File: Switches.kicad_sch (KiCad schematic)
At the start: 36 parts, among them SW10 SW_SPST, SW11 SW_SPST, SW12 SW_SPST, SW13 SW_SPST, SW14 SW_SPST, SW15 SW_SPST, SW16 SW_SPST, SW17 SW_SPST, SW18 Rotary, SW19 Rotary, SW2 SW_SPST, SW3 SW_SPST, SW4 SW_SPST, SW5 SW_SPST, SW6 SW_SPST, SW7 SW_SPST, SW8 SW_SPST, SW9 SW_SPST

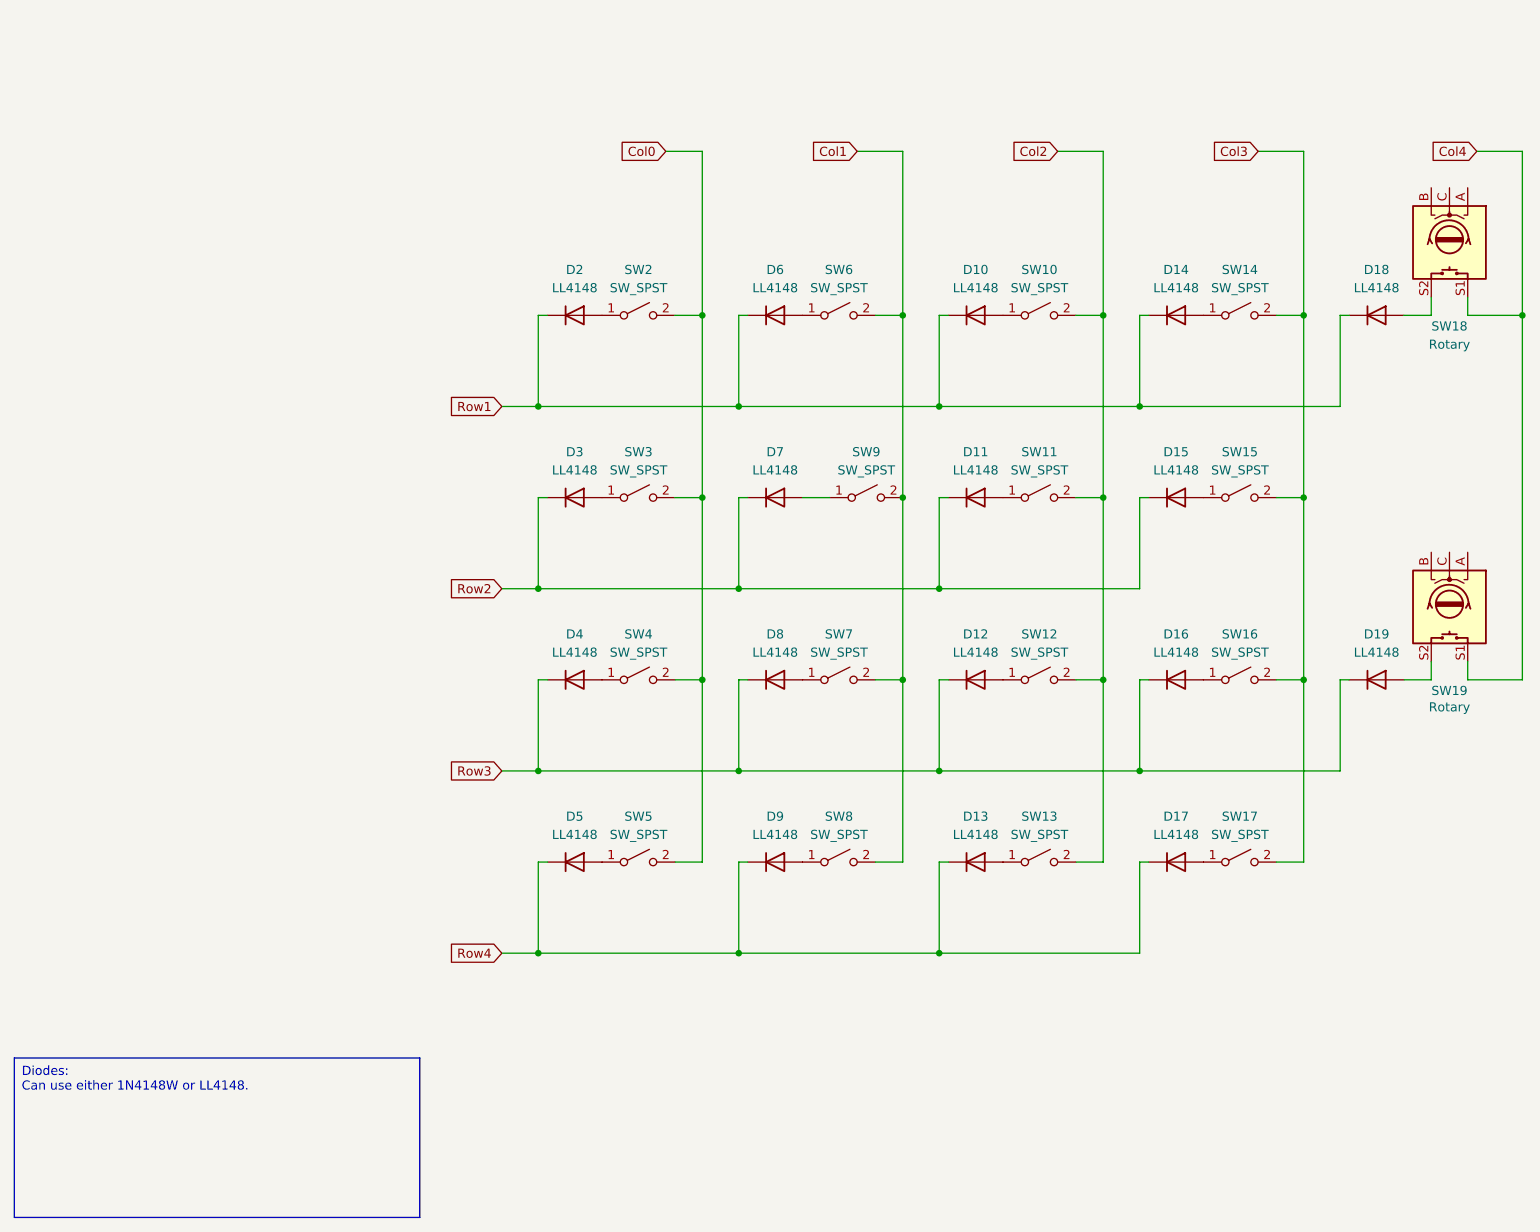
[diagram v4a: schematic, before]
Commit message: Select last few components, add and cleanup footprints
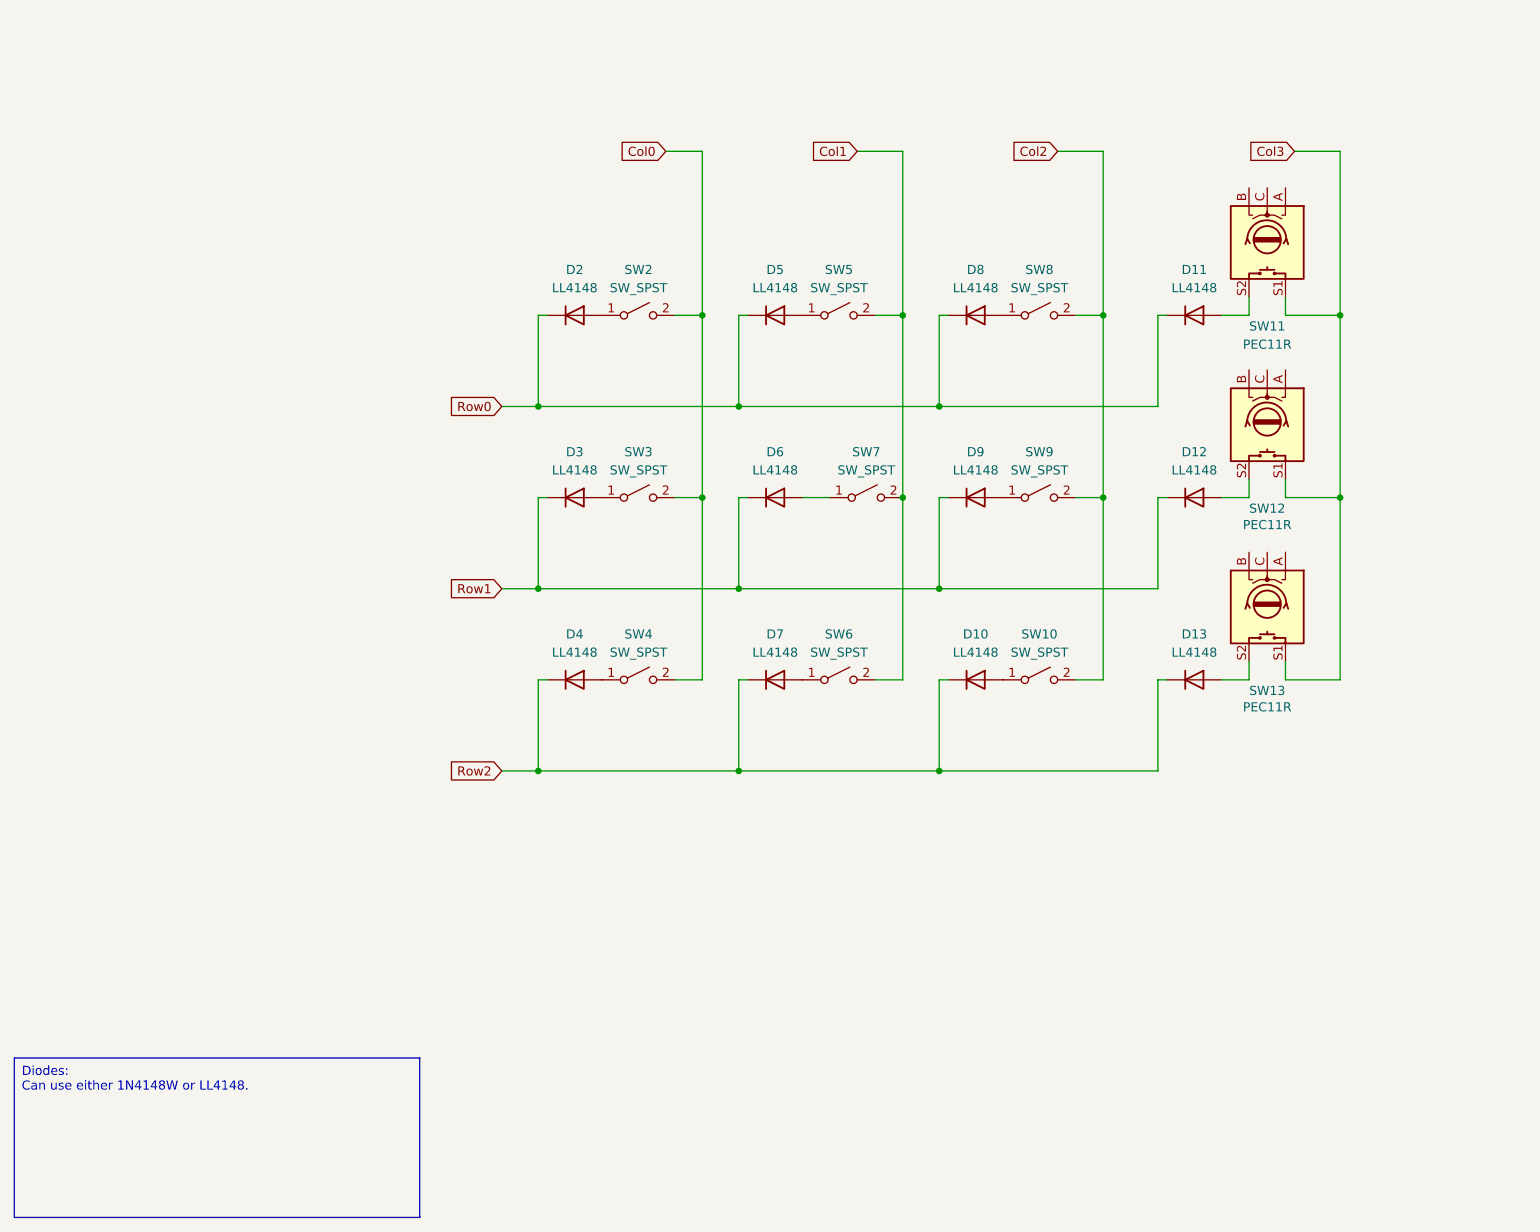
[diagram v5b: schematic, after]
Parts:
- removed D13, D14, D15, D16, D17, D5, D9: LL4148, Diode_SMD:D_MiniMELF, symbol Diode:LL4148
- removed SW13, SW14, SW15, SW16, SW17, SW5, SW8: SW_SPST, PCM_Switch_Keyboard_Cherry_MX:SW_Cherry_MX_PCB_1.00u, symbol Switch:SW_SPST
- added D12: LL4148, Diode_SMD:D_MiniMELF, symbol Diode:LL4148
- added SW12: PEC11R, Mad_Footprints:RotaryEncoder_Bourns_Vertical_PEC12R-3x17F-Sxxxx, symbol Device:RotaryEncoder_Switch
- SW10: renamed from SW12; footprint PCM_Switch_Keyboard_Cherry_MX:SW_Cherry_MX_PCB_1.00u -> Mad_Footprints:SW_Hotswap_Kailh_MX_1.00u
- SW11: renamed from SW18; value Rotary -> PEC11R; footprint (none) -> Mad_Footprints:RotaryEncoder_Bourns_Vertical_PEC12R-3x17F-Sxxxx; MPN (none) -> PEC11R-4215F-S0024; Manufacturer (none) -> Bourns Inc.; Price (none) -> $3.37; Rating (none) -> ROTARY ENCODER MECHANICAL 24PPR; Supplier (none) -> Digikey; Supplier PN (none) -> PEC11R-4215F-S0024-ND
- SW13: renamed from SW19; value Rotary -> PEC11R; footprint (none) -> Mad_Footprints:RotaryEncoder_Bourns_Vertical_PEC12R-3x17F-Sxxxx; MPN (none) -> PEC11R-4215F-S0024; Manufacturer (none) -> Bourns Inc.; Price (none) -> $3.37; Rating (none) -> ROTARY ENCODER MECHANICAL 24PPR; Supplier (none) -> Digikey; Supplier PN (none) -> PEC11R-4215F-S0024-ND
- SW2, SW3, SW4: footprint PCM_Switch_Keyboard_Cherry_MX:SW_Cherry_MX_PCB_1.00u -> Mad_Footprints:SW_Hotswap_Kailh_MX_1.00u
- SW5: renamed from SW6; footprint PCM_Switch_Keyboard_Cherry_MX:SW_Cherry_MX_PCB_1.00u -> Mad_Footprints:SW_Hotswap_Kailh_MX_1.00u
- SW6: renamed from SW7; footprint PCM_Switch_Keyboard_Cherry_MX:SW_Cherry_MX_PCB_1.00u -> Mad_Footprints:SW_Hotswap_Kailh_MX_1.00u
- SW7: renamed from SW9; footprint PCM_Switch_Keyboard_Cherry_MX:SW_Cherry_MX_PCB_1.00u -> Mad_Footprints:SW_Hotswap_Kailh_MX_1.00u
- SW8: renamed from SW10; footprint PCM_Switch_Keyboard_Cherry_MX:SW_Cherry_MX_PCB_1.00u -> Mad_Footprints:SW_Hotswap_Kailh_MX_1.00u
- SW9: renamed from SW11; footprint PCM_Switch_Keyboard_Cherry_MX:SW_Cherry_MX_PCB_1.00u -> Mad_Footprints:SW_Hotswap_Kailh_MX_1.00u
- renumbered D12 to D10, D18 to D11, D19 to D13, D6 to D5, D7 to D6, D8 to D7, D10 to D8, D11 to D9
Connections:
- net Col4 is gone; now on net Col3: SW11.S1, SW13.S1
- net Row3 is gone; now on net Row2: D10.1 (K), D13.1 (K), D4.1 (K), D7.1 (K)
- net Col3: now also SW12.S1
- net Row1: now also D3.1 (K), D6.1 (K), D9.1 (K), D12.1 (K); no longer D11.1 (K), D2.1 (K), D5.1 (K), D8.1 (K)
- net Row2: no longer D3.1 (K), D6.1 (K), D9.1 (K)
- new net: D12.2 (A), SW12.S2
- new net Row0: D11.1 (K), D2.1 (K), D5.1 (K), D8.1 (K)
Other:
- moved on the sheet: D11, D13, SW11, SW13

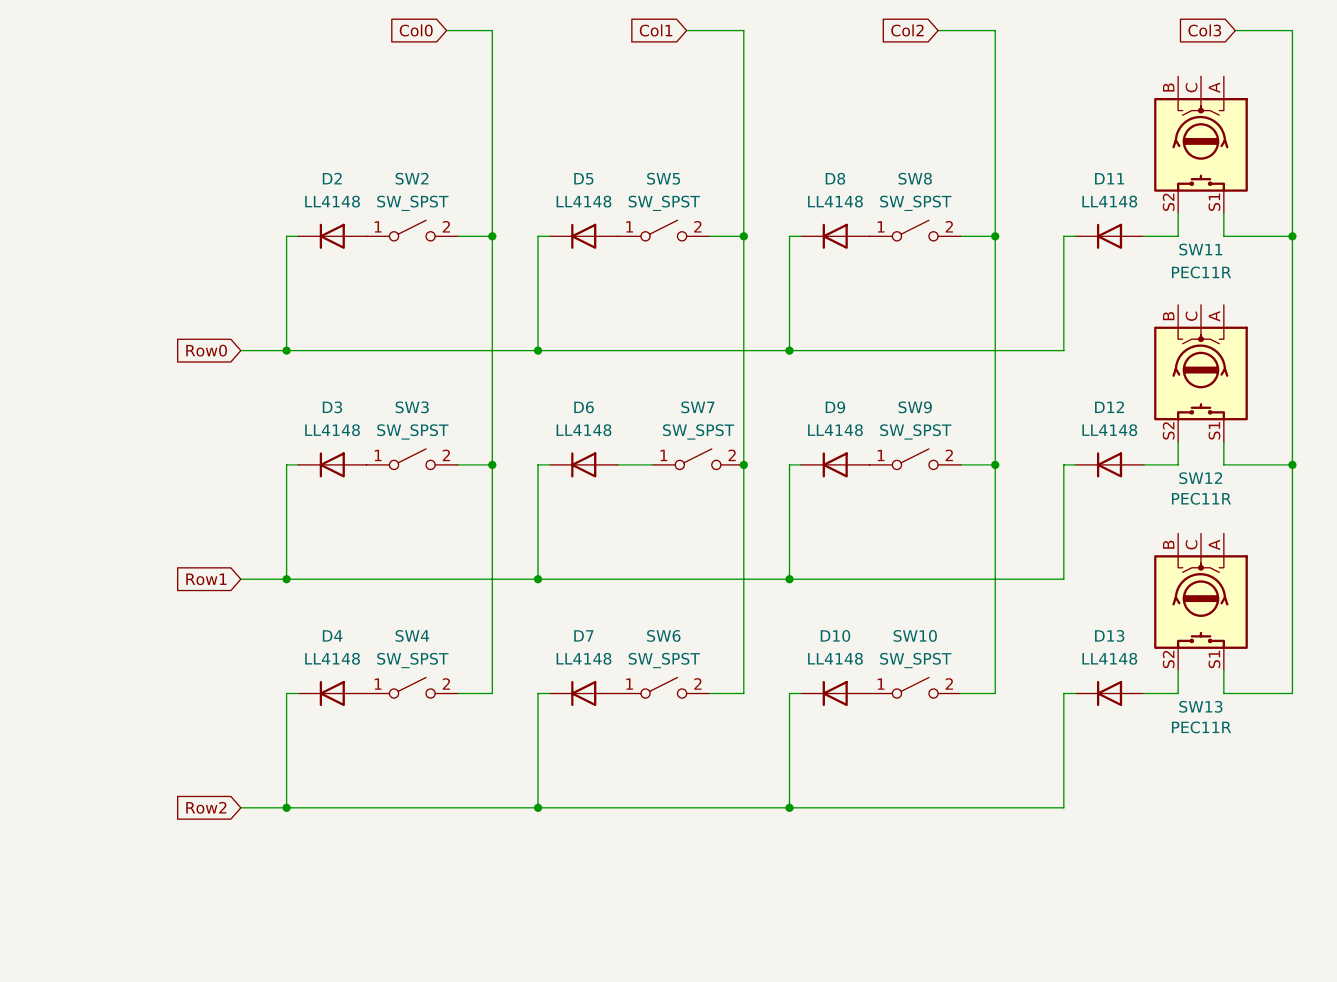
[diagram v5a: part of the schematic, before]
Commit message: Update lib, finish off rotary encoder schematic, reselect diode for reset circuit
Update RP2040, rename bom only footprint, add mechanical footprint. Add PCB symbol
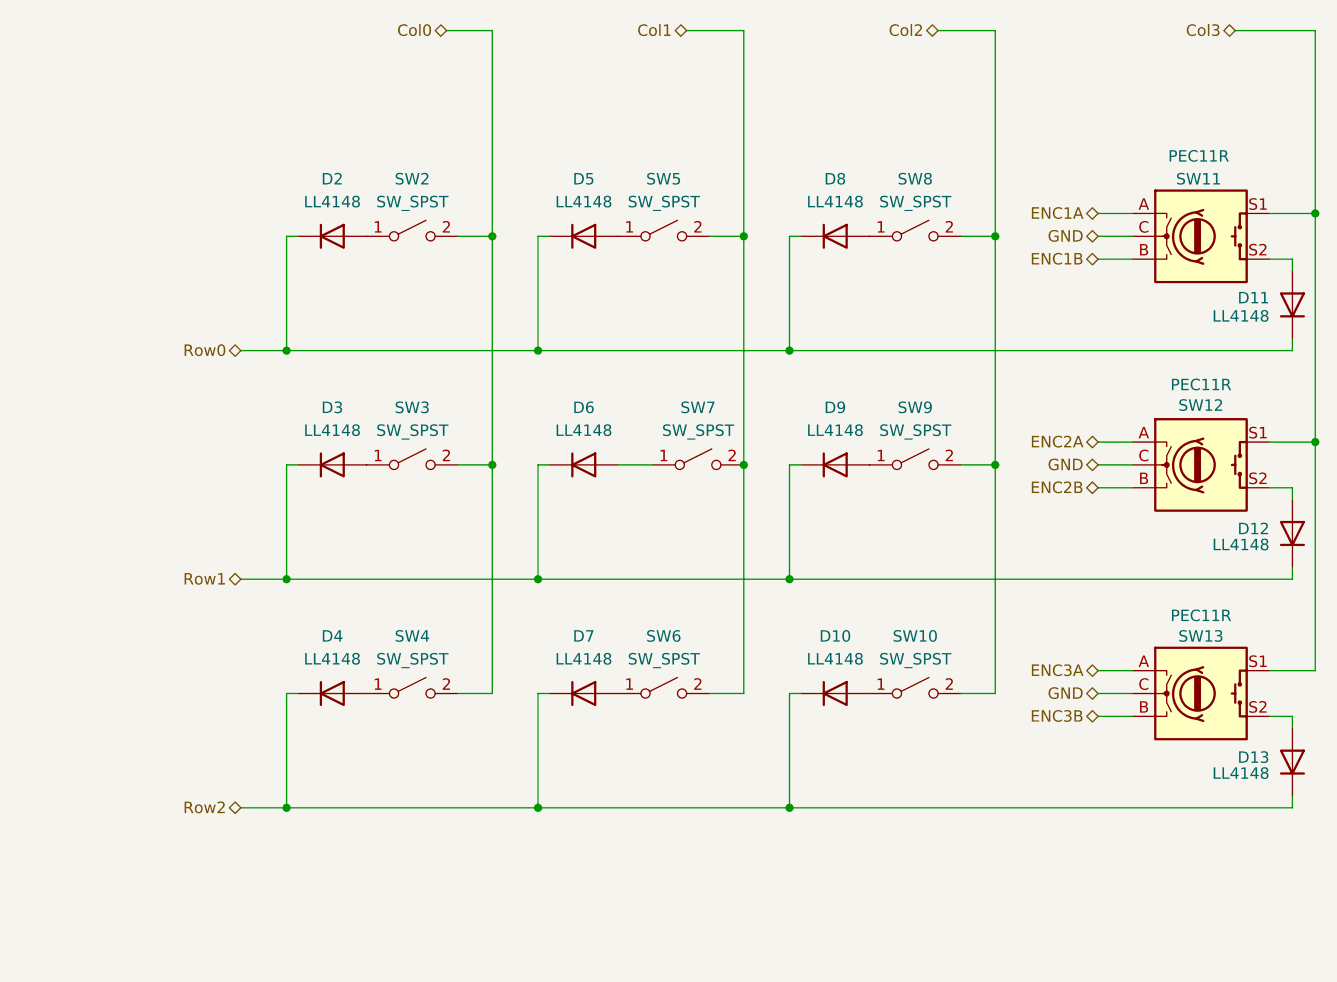
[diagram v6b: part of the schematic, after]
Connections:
- net ENC2A: now reaches SW12.A
- net ENC2B: now reaches SW12.B
- net GND: now reaches SW12.C
- net GND: now also SW11.C, SW13.C
- net ENC1A: now reaches SW11.A
- net ENC1B: now reaches SW11.B
- net ENC3A: now reaches SW13.A
- net ENC3B: now reaches SW13.B
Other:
- moved on the sheet: D11, D12, D13, SW11, SW12, SW13

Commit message: Finish off rotary encoders, add EMC zone for USB, fix few remaining lib links, fix DRC
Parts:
- added C20, C21, C22, C23, C24, C25: 100nF, Capacitor_SMD:C_0402_1005Metric, symbol Device:C_Small
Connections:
- net ENC1A: now also C20.1
- net ENC1B: now also C21.2
- net ENC2A: now also C22.1
- net ENC2B: now also C23.2
- net ENC3A: now also C24.1
- net ENC3B: now also C25.2
- net GND: now also C20.2, C21.1, C22.2, C23.1, C24.2, C25.1
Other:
- moved on the sheet: D10, D11, D2, D3, D4, D5, D6, D7, D8, D9, SW10, SW11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

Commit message: Refactor, cleanup, add todo list, update metadata on BOM
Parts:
- removed C22, C23, C24, C25: 100nF, Capacitor_SMD:C_0402_1005Metric, symbol Device:C_Small
- removed D11, D12, D13: LL4148, Diode_SMD:D_MiniMELF, symbol Diode:LL4148
- removed SW12, SW13: PEC11R, Mad_Footprints:RotaryEncoder_Bourns_Vertical_PEC12R-3x17F-Sxxxx, symbol Device:RotaryEncoder_Switch
- removed SW2, SW5, SW8: SW_SPST, Mad_Footprints:SW_Hotswap_Kailh_MX_1.00u, symbol Switch:SW_SPST
- added C26, C27, C28, C29: 100nF, Capacitor_SMD:C_0402_1005Metric, symbol Device:C_Small
- added D11, D12, D13, D14, D15, D16: WS2812C-2020, Mad_Footprints:SK6812_mini_e, symbol Mad_Symbols:SK6812_Mini_E
- added SW2, SW5: PEC11R, Mad_Footprints:RotaryEncoder_Bourns_Vertical_PEC12R-3x17F-Sxxxx, symbol Device:RotaryEncoder_Switch
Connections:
- net Col3 is gone; now on net Col2: SW11.S1
- net Col0: now also SW2.S1
- net Col1: now also SW5.S1
- net ENC1A: now also C28.1, SW2.A; no longer C20.1, SW11.A
- net ENC1B: now also C29.2, SW2.B; no longer C21.2, SW11.B
- net ENC2A: now also C26.1, SW5.A
- net ENC2B: now also C27.2, SW5.B
- net ENC3A: now also C20.1, SW11.A
- net ENC3B: now also C21.2, SW11.B
- net GND: now also C26.2, C27.1, C28.2, C29.1, D11.3 (GND), D12.3 (GND), D13.3 (GND), D14.3 (GND), D15.3 (GND), D16.3 (GND), SW2.C, SW5.C
- net at D2.2 (A): now also SW2.S2
- net at D5.2 (A): now also SW5.S2
- net at SW11.S2: now also D8.2 (A)
- new net: D11.2 (DOUT), D12.4 (DIN)
- new net: D15.2 (DOUT), D16.4 (DIN)
- new net: D12.2 (DOUT), D13.4 (DIN)
- new net: D14.2 (DOUT), D15.4 (DIN)
- new net: D13.2 (DOUT), D14.4 (DIN)
- new net 5V: D11.1 (VDD), D12.1 (VDD), D13.1 (VDD), D14.1 (VDD), D15.1 (VDD), D16.1 (VDD)
- new net DIN: D11.4 (DIN)
- new net DOUT: D16.2 (DOUT)
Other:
- moved on the sheet: C20, C21, D10, D3, D4, D6, D7, D8, D9, SW10, SW11, SW3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
